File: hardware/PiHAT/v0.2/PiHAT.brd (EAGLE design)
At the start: 65 x 56.5 mm, 47 parts, among them J1 FTDI, J3 ISP, U1 ATMEGA328P, U2 TSL2561, U3 OPA344, U4 MPL115A, U6 ADMP401, U7 SHT31-DIS, Y1 16MHZ

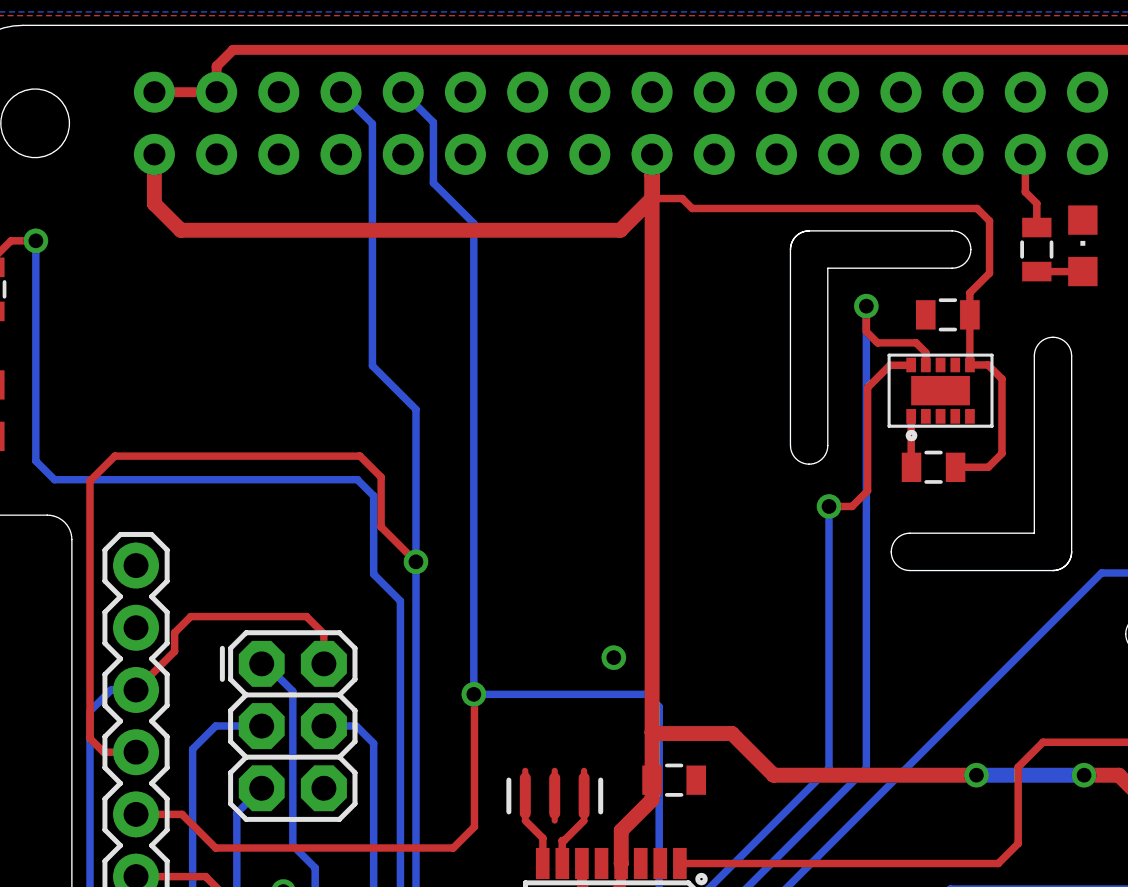
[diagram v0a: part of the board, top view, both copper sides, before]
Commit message: Power trace adjustment
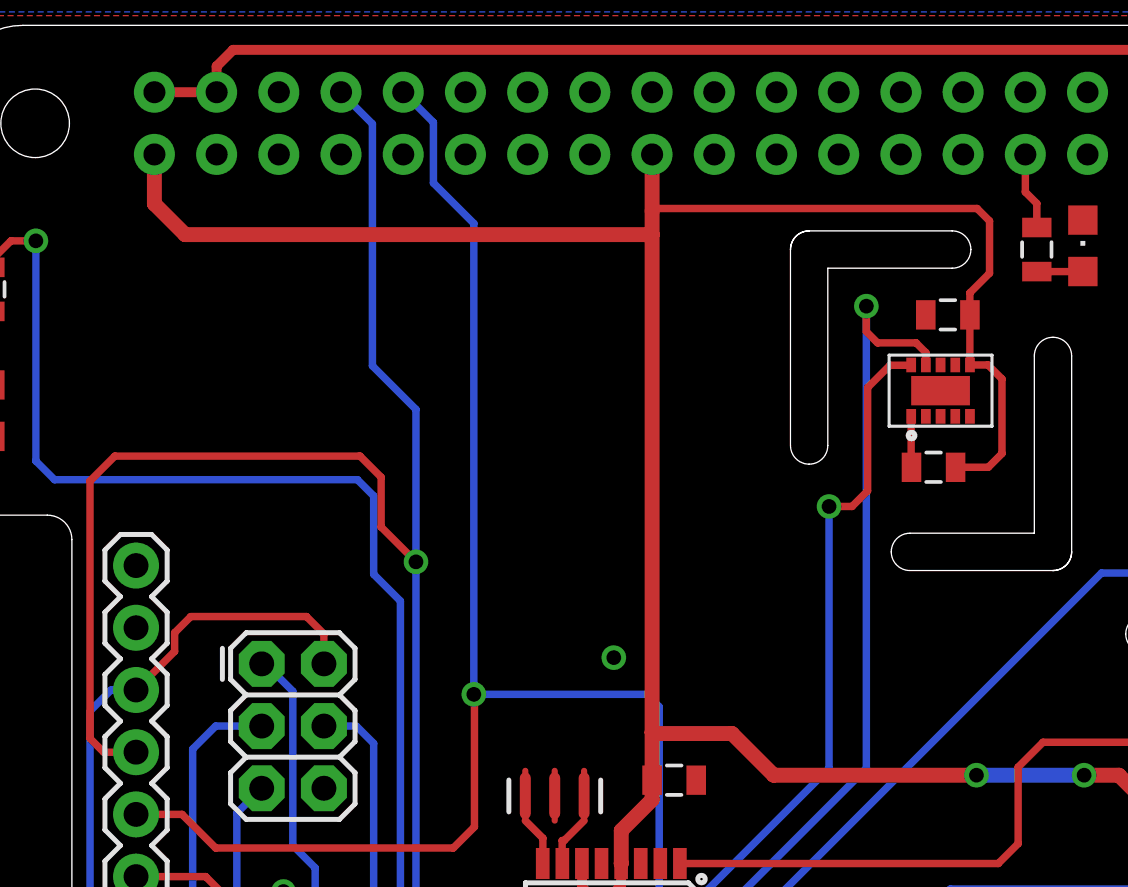
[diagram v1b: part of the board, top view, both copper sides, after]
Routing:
- net VCC: track 242.0 -> 240.4 mm
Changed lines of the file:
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@@
 <wire x1="36.9932" y1="5.9944" x2="37.014" y2="6.0152" width="0.3048" layer="1"/>
 <wire x1="8.37" y1="49.96" x2="8.37" y2="47.9418" width="0.6096" layer="1"/>
-<wire x1="8.37" y1="47.9418" x2="9.4488" y2="46.863" width="0.6096" layer="1"/>
+<wire x1="8.37" y1="47.9418" x2="9.6266" y2="46.6852" width="0.6096" layer="1"/>
 <wire x1="13.049" y1="3.798" x2="10.818" y2="3.798" width="0.3048" layer="1"/>
 <wire x1="10.818" y1="3.798" x2="10.795" y2="3.821" width="0.3048" layer="1"/>
@@
 <wire x1="56.0578" y1="16.8656" x2="57.762" y2="16.8656" width="0.3048" layer="1"/>
 <wire x1="57.762" y1="16.8656" x2="57.7812" y2="16.8464" width="0.3048" layer="1"/>
-<wire x1="28.69" y1="49.96" x2="28.69" y2="49.1236" width="0.6096" layer="1"/>
 <via x="41.9354" y="24.6126" extent="1-16" drill="0.6"/>
-<wire x1="28.69" y1="49.1236" x2="28.69" y2="48.1584" width="0.6096" layer="1"/>
-<wire x1="9.4488" y1="46.863" x2="27.3946" y2="46.863" width="0.6096" layer="1"/>
 <wire x1="46.3296" y1="24.6126" x2="47.752" y2="24.6126" width="0.6096" layer="1"/>
 <wire x1="47.752" y1="24.6126" x2="48.4632" y2="23.9014" width="0.6096" layer="1"/>
@@
 <wire x1="42.418" y1="37.1856" x2="41.0828" y2="37.1856" width="0.3048" layer="1"/>
 <wire x1="46.3296" y1="24.6126" x2="41.9354" y2="24.6126" width="0.6096" layer="16"/>
-<wire x1="27.3946" y1="46.863" x2="28.69" y2="48.1584" width="0.6096" layer="1"/>
-<wire x1="41.9608" y1="47.752" x2="30.3276" y2="47.752" width="0.3048" layer="1"/>
-<wire x1="30.3276" y1="47.752" x2="29.9212" y2="48.1584" width="0.3048" layer="1"/>
-<wire x1="29.9212" y1="48.1584" x2="28.69" y2="48.1584" width="0.3048" layer="1"/>
 <wire x1="28.691" y1="24.4094" x2="28.691" y2="26.3652" width="0.6096" layer="1"/>
-<wire x1="28.691" y1="26.3652" x2="28.691" y2="49.1226" width="0.6096" layer="1"/>
-<wire x1="28.691" y1="49.1226" x2="28.69" y2="49.1236" width="0.6096" layer="1"/>
 <wire x1="41.9354" y1="24.6126" x2="33.655" y2="24.6126" width="0.6096" layer="1"/>
 <wire x1="33.655" y1="24.6126" x2="31.9532" y2="26.3144" width="0.6096" layer="1"/>
@@
 <wire x1="14.5796" y1="31.0896" x2="15.2908" y2="30.3784" width="0.3048" layer="1"/>
 <wire x1="15.2908" y1="30.3784" x2="15.2908" y2="29.1592" width="0.3048" layer="1"/>
+<wire x1="28.691" y1="47.6504" x2="28.691" y2="49.959" width="0.6096" layer="1"/>
+<wire x1="28.691" y1="49.959" x2="28.69" y2="49.96" width="0.6096" layer="1"/>
+<wire x1="41.9608" y1="47.752" x2="28.7926" y2="47.752" width="0.3048" layer="1"/>
+<wire x1="28.7926" y1="47.752" x2="28.691" y2="47.6504" width="0.3048" layer="1"/>
+<wire x1="28.691" y1="47.6504" x2="28.691" y2="46.6852" width="0.6096" layer="1"/>
+<wire x1="28.691" y1="46.6852" x2="28.691" y2="26.3652" width="0.6096" layer="1"/>
+<wire x1="9.6266" y1="46.6852" x2="28.691" y2="46.6852" width="0.6096" layer="1"/>
 </signal>
 <signal name="D5">

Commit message: updating sch for cleaner bom
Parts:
- renumbered U$1 to U8
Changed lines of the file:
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@@
 </autorouter>
 <elements>
-<element name="RPI1" library="microbuilder" package="PI_HAT_SLOTS" value="RASPBERRYPI_BPLUS_HATSLOTS" x="0" y="-1.27" smashed="yes"/>
+<element name="RPI1" library="microbuilder" package="PI_HAT_SLOTS" value="RASPBERRYPI_BPLUS_HATSLOTS" x="0" y="-1.27" smashed="yes">
+<attribute name="NO_BOM" value="TRUE" x="0" y="-1.27" size="1.778" layer="27" display="off"/>
+</element>
 <element name="U1" library="SparkFun-DigitalIC" package="TQFP32-08" value="ATMEGA328P" x="27.0256" y="16.7132" smashed="yes" rot="R270">
 <attribute name="MF" value="" x="61.1886" y="41.8592" size="1.778" layer="27" rot="R270" display="off"/>
@@
 <element name="LED2" library="adafruit" package="CHIPLED_0805" value="" x="1.651" y="39.497" smashed="yes" rot="R180">
 <attribute name="MF" value="" x="69.596" y="-3.81" size="1.778" layer="27" rot="R180" display="off"/>
-<attribute name="MPN" value="" x="69.596" y="-3.81" size="1.778" layer="27" rot="R180" display="off"/>
-<attribute name="OC_NEWARK" value="unknown" x="69.596" y="-3.81" size="1.778" layer="27" rot="R180" display="off"/>
+<attribute name="MPN" value="LY L29K-H1K2-26-Z" x="69.596" y="-3.81" size="1.778" layer="27" rot="R180" display="off"/>
 <attribute name="VALUE" x="-0.889" y="40.767" size="1.27" layer="27" rot="R270"/>
 <attribute name="DIGIKEY#" value="475-1196-1-ND" x="1.651" y="39.497" size="1.778" layer="27" rot="R180" display="off"/>
@@
 <attribute name="PROD_ID" value="COMP-12310" x="74.422" y="146.812" size="1.778" layer="27" rot="R270" display="off"/>
 <attribute name="NAME" x="53.975" y="31.6992" size="0.8128" layer="121" font="vector"/>
+<attribute name="MPN" value="MiCS-4514" x="56.642" y="37.592" size="1.778" layer="27" rot="R270" display="off"/>
+<attribute name="MANF" value="SensorTech" x="56.642" y="37.592" size="1.778" layer="27" rot="R270" display="off"/>
 </element>
 <element name="R14" library="SparkFun-Passives" package="0805" value="47K" x="58.8264" y="44.0436" smashed="yes" rot="R180">
@@
 <attribute name="VALUE" x="54.6862" y="45.466" size="0.8128" layer="121" font="vector" rot="R90"/>
 </element>
-<element name="U$1" library="CCS811" package="LGA" value="CCS811" x="42.4688" y="38.9636" smashed="yes" rot="R90">
+<element name="U8" library="CCS811" package="LGA" value="CCS811" x="42.4688" y="38.9636" smashed="yes" rot="R90">
 <attribute name="VALUE" x="37.0078" y="42.545" size="0.8128" layer="121" font="vector" rot="R270"/>
+<attribute name="MANF" value="AMS" x="42.4688" y="38.9636" size="1.778" layer="27" rot="R90" display="off"/>
+<attribute name="MPN" value="CCS811" x="42.4688" y="38.9636" size="1.778" layer="27" rot="R90" display="off"/>
 </element>
 <element name="R9" library="SparkFun-Passives" package="0805" value="100K" x="40.1828" y="37.1856" smashed="yes" rot="R180">
@@
 <attribute name="VALUE" x="9.2964" y="35.8394" size="0.8128" layer="121" font="vector" rot="R180"/>
 <attribute name="MPN" value="FT231XS-R" x="7.62" y="20.4724" size="1.778" layer="27" rot="R90" display="off"/>
+<attribute name="DIGIKEY#" value="768-1129-1-ND" x="7.62" y="20.4724" size="1.778" layer="27" rot="R90" display="off"/>
 </element>
 <element name="J3" library="SparkFun-Connectors" package="2X3" value="ISP" x="12.7508" y="29.1592" smashed="yes" rot="R270">
 <attribute name="VALUE" x="13.3096" y="31.1658" size="0.8128" layer="121" font="vector"/>
+<attribute name="NO_BOM" value="TRUE" x="12.7508" y="29.1592" size="1.778" layer="27" rot="R270" display="off"/>
 </element>
 </elements>
@@
 <wire x1="15.4178" y1="0.3302" x2="15.9004" y2="-0.1524" width="0.3048" layer="1"/>
 <wire x1="15.9004" y1="-0.1524" x2="29.7688" y2="-0.1524" width="0.3048" layer="1"/>
-<contactref element="U$1" pad="9"/>
+<contactref element="U8" pad="9"/>
 <wire x1="37.4396" y1="43.7642" x2="37.4396" y2="24.892" width="0.3048" layer="16"/>
 <wire x1="39.8688" y1="41.3636" x2="39.8688" y2="41.8684" width="0.3048" layer="1"/>
@@
 <wire x1="18.3388" y1="-0.1524" x2="20.9296" y2="-0.1524" width="0.3048" layer="16"/>
 <wire x1="20.9296" y1="-0.1524" x2="22.2758" y2="1.1938" width="0.3048" layer="16"/>
-<contactref element="U$1" pad="10"/>
+<contactref element="U8" pad="10"/>
 <wire x1="35.9156" y1="35.5854" x2="35.9156" y2="24.892" width="0.3048" layer="16"/>
 <wire x1="35.9156" y1="24.892" x2="26.8224" y2="15.7988" width="0.3048" layer="16"/>
@@
 <via x="27.1272" y="29.4132" extent="1-16" drill="0.6"/>
 <contactref element="LED_26" pad="C"/>
-<contactref element="U$1" pad="11"/>
+<contactref element="U8" pad="11"/>
 <contactref element="C5" pad="2"/>
 <contactref element="LED_05" pad="C"/>
@@
 <wire x1="28.69" y1="23.61" x2="28.69" y2="24.4084" width="0.6096" layer="1"/>
 <wire x1="28.69" y1="24.4084" x2="28.691" y2="24.4094" width="0.6096" layer="1"/>
-<contactref element="U$1" pad="6"/>
+<contactref element="U8" pad="6"/>
 <contactref element="C5" pad="1"/>
 <contactref element="R9" pad="1"/>
@@
 </signal>
 <signal name="N$16">
-<contactref element="U$1" pad="1"/>
+<contactref element="U8" pad="1"/>
 <contactref element="R9" pad="2"/>
 <wire x1="39.2688" y1="39.2636" x2="39.2688" y2="37.1996" width="0.3048" layer="1"/>

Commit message: adding details to aid in fabrication
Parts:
- removed LED_05: (no value), adafruit:CHIPLED_0805
- added LED1: (no value), adafruit:CHIPLED_0805
- moved LED2 45.1 mm to (46.3, 46.2), turned to 0 degrees
- renumbered LED_26 to LED3
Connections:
- net GND: now also LED1.C; no longer LED_05.C
- net N$3: now also LED1.A; no longer LED2.A
- net N$6: now also LED2.A; no longer LED_05.A
